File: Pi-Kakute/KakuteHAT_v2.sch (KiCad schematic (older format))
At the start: 52 parts, among them J1 40HAT, J10 Ext_Switch, J12 FC_Socket, J2 Conn_01x02, J3 I2C, J4 Mout, J6 RC_IN, J7 GPS2, J8 Power_Pad, J9 FC_Socket2, Q1 DMMT5401, Q2 DMG2305UX, SW1 Kakute Power Switch, SW2 Pi Power Switch, U1 TPS22810, U2 TPS709, U3 KakuteF4_V2, U4 TPS54331DR, U5 NC7SZ00P5X, U6 CAT24C32

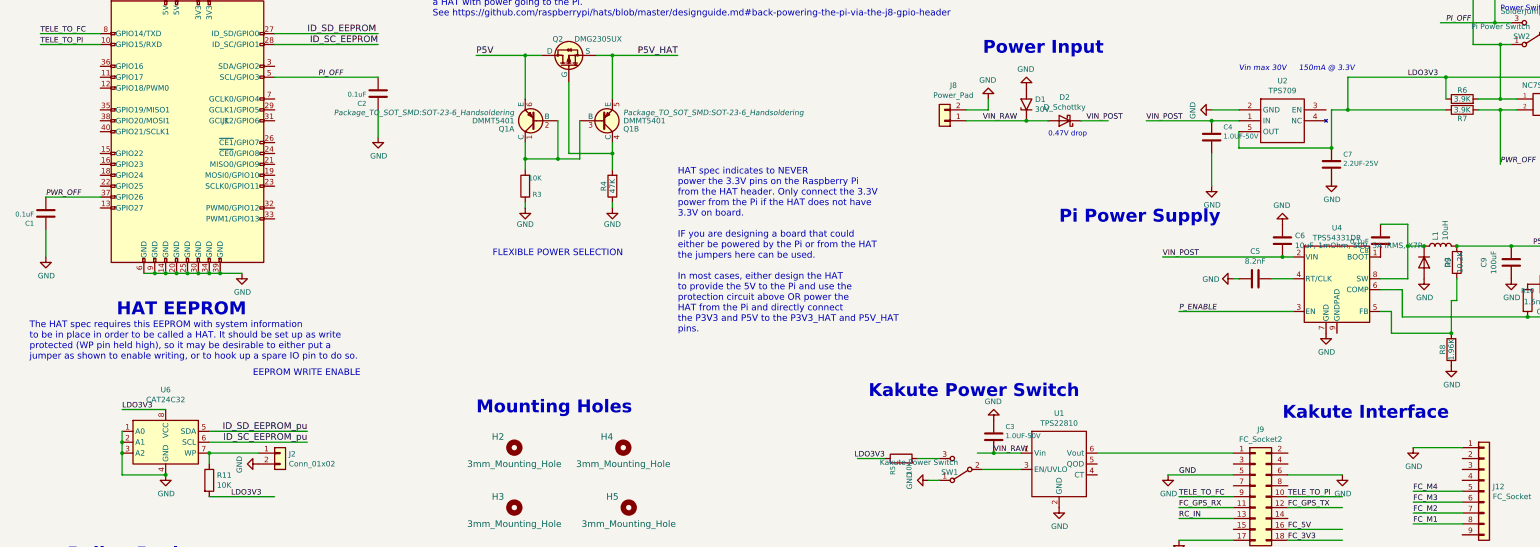
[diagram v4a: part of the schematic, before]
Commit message: Pi-Kakute: Label Cleanup
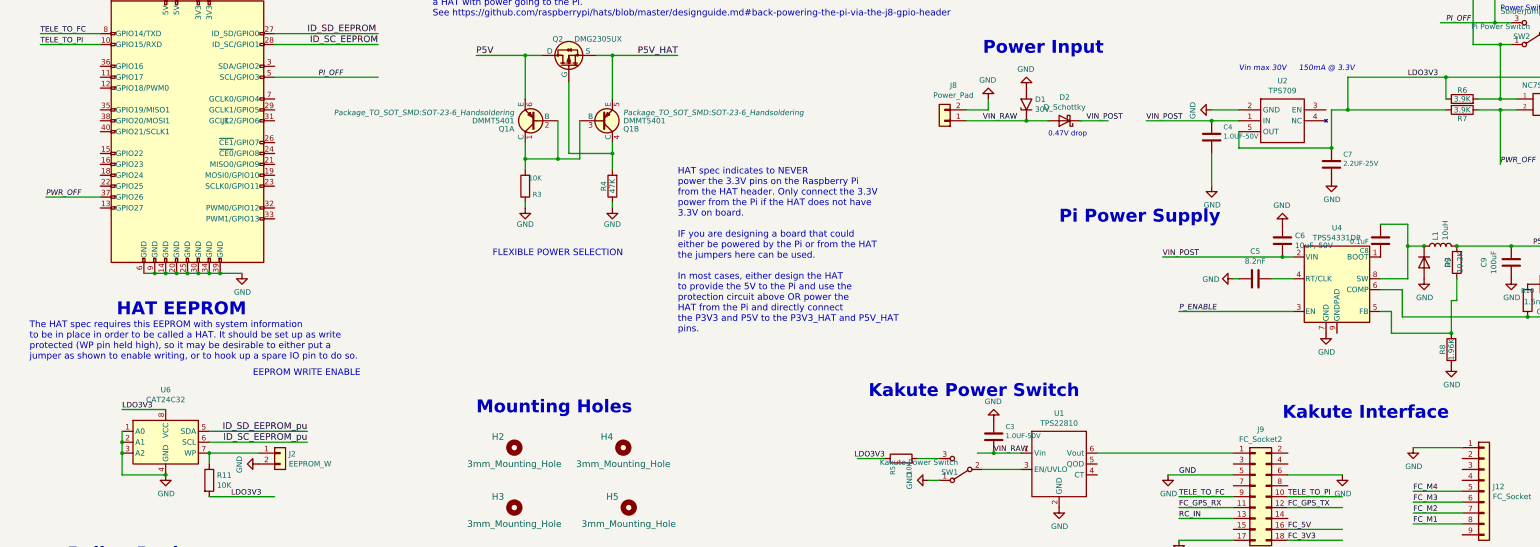
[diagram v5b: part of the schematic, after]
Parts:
- removed C1, C2: 0.1uF, Capacitor_SMD:C_0402_1005Metric, symbol Device:C
- C4: MPN CC0805KKX7R8BB105 -> CC0805KKX7R9BB105; SPN 311-1456-1-ND -> 311-1886-1-ND
- C6: value 10uF, 1mOhm, 50V, 5A IRMS, X7R -> 10uF, 50V
- H1, H2, H3, H4, H5, J10, J3, JP1: MFR (none) -> N/A; MPN (none) -> N/A; SPN (none) -> N/A; SPR (none) -> N/A
- J2: value Conn_01x02 -> EEPROM_W; MFR (none) -> N/A; MPN (none) -> N/A; SPN (none) -> N/A; SPR (none) -> N/A
- U2: MFR (none) -> TI; MPN (none) -> TPS70933DBVR; SPN (none) -> 296-35483-1-ND; SPR (none) -> Digikey
- U3: MFR HolyBro -> N/A; MPN (none) -> N/A; SPN (none) -> N/A; SPR (none) -> N/A
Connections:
- wire segments 168 -> 166
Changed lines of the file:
@@
 F 2 "MountingHole:MountingHole_3.2mm_M3_ISO7380" H 5550 6000 60  0001 C CNN
 F 3 "" H 5550 6000 60  0001 C CNN
-F 4 "~" H 0   0   50  0001 C CNN "MFR"
-F 5 "~" H 0   0   50  0001 C CNN "MPN"
+F 4 "N/A" H 0   0   50  0001 C CNN "MFR"
+F 5 "N/A" H 0   0   50  0001 C CNN "MPN"
+F 6 "N/A" H 5650 6000 50  0001 C CNN "SPN"
+F 7 "N/A" H 5650 6000 50  0001 C CNN "SPR"
 	1    5650 6000
 	1    0    0    -1
@@
 F 2 "MountingHole:MountingHole_3.2mm_M3_ISO7380" H 6550 6000 60  0001 C CNN
 F 3 "" H 6550 6000 60  0001 C CNN
-F 4 "~" H 0   0   50  0001 C CNN "MFR"
-F 5 "~" H 0   0   50  0001 C CNN "MPN"
+F 4 "N/A" H 0   0   50  0001 C CNN "MFR"
+F 5 "N/A" H 0   0   50  0001 C CNN "MPN"
+F 6 "N/A" H 6650 6000 50  0001 C CNN "SPN"
+F 7 "N/A" H 6650 6000 50  0001 C CNN "SPR"
 	1    6650 6000
 	1    0    0    -1
@@
 F 2 "MountingHole:MountingHole_3.2mm_M3_ISO7380" H 5550 6550 60  0001 C CNN
 F 3 "" H 5550 6550 60  0001 C CNN
-F 4 "~" H 0   0   50  0001 C CNN "MFR"
-F 5 "~" H 0   0   50  0001 C CNN "MPN"
+F 4 "N/A" H 0   0   50  0001 C CNN "MFR"
+F 5 "N/A" H 0   0   50  0001 C CNN "MPN"
+F 6 "N/A" H 5650 6550 50  0001 C CNN "SPN"
+F 7 "N/A" H 5650 6550 50  0001 C CNN "SPR"
 	1    5650 6550
 	1    0    0    -1
@@
 F 2 "MountingHole:MountingHole_3.2mm_M3_ISO7380" H 6600 6550 60  0001 C CNN
 F 3 "" H 6600 6550 60  0001 C CNN
-F 4 "~" H 0   0   50  0001 C CNN "MFR"
-F 5 "~" H 0   0   50  0001 C CNN "MPN"
+F 4 "N/A" H 0   0   50  0001 C CNN "MFR"
+F 5 "N/A" H 0   0   50  0001 C CNN "MPN"
+F 6 "N/A" H 6700 6550 50  0001 C CNN "SPN"
+F 7 "N/A" H 6700 6550 50  0001 C CNN "SPR"
 	1    6700 6550
 	1    0    0    -1
@@
 F 3 "" H 12050 3150 50  0001 C CNN
 F 4 "Yageo" H 150 -200 50  0001 C CNN "MFR"
-F 5 "CC0805KKX7R8BB105" H 150 -200 50  0001 C CNN "MPN"
-F 6 "311-1456-1-ND" H 150 -200 50  0001 C CNN "SPN"
+F 5 "CC0805KKX7R9BB105" H 150 -200 50  0001 C CNN "MPN"
+F 6 "311-1886-1-ND" H 150 -200 50  0001 C CNN "SPN"
 F 7 "OPL" H 150 -200 50  0001 C CNN "SPR"
 F 8 "302010179" H 400 -100 50  0001 C CNN "SKU"
@@
 F 2 "Kakute:Kakute F4 V2_NoPin" H 13250 7650 50  0001 C CNN
 F 3 "" H 13250 7650 50  0001 C CNN
-F 4 "HolyBro" H 550 1550 50  0001 C CNN "MFR"
-F 5 "~" H 0   0   50  0001 C CNN "MPN"
+F 4 "N/A" H 550 1550 50  0001 C CNN "MFR"
+F 5 "N/A" H 0   0   50  0001 C CNN "MPN"
+F 6 "N/A" H 12950 7800 50  0001 C CNN "SPN"
+F 7 "N/A" H 12950 7800 50  0001 C CNN "SPR"
 	1    12950 7800
 	1    0    0    -1
@@
 Wire Wire Line
 	1850 2300 1300 2300
-$Comp
-L Device:C C2
-U 1 1 5C476D9B
-P 4400 2750
-F 0 "C2" H 4508 2842 45  0000 L CNN
-F 1 "0.1uF" H 4508 2758 45  0000 L CNN
-F 2 "Capacitor_SMD:C_0402_1005Metric" H 4400 3000 20  0001 C CNN
-F 3 "" H 4400 2750 50  0001 C CNN
-F 4 "OPL" H -7500 -600 50  0001 C CNN "SPR"
-F 5 "CC0402KRX7R7BB104" H -6500 -1350 50  0001 C CNN "MPN"
-F 6 "302010138" H 0   0   50  0001 C CNN "SKU"
-F 7 "311-1338-1-ND" H 0   0   50  0001 C CNN "SPN"
-F 8 "Yageo" H 0   0   50  0001 C CNN "MFR"
-	1    4400 2750
-	-1   0    0    1
-$EndComp
-$Comp
-L Device:C C1
-U 1 1 5C476E84
-P 1350 3850
-F 0 "C1" H 1458 3942 45  0000 L CNN
-F 1 "0.1uF" H 1458 3858 45  0000 L CNN
-F 2 "Capacitor_SMD:C_0402_1005Metric" H 1350 4100 20  0001 C CNN
-F 3 "" H 1350 3850 50  0001 C CNN
-F 4 "OPL" H -10550 500 50  0001 C CNN "SPR"
-F 5 "CC0402KRX7R7BB104" H -9550 -250 50  0001 C CNN "MPN"
-F 6 "302010138" H 0   0   50  0001 C CNN "SKU"
-F 7 "311-1338-1-ND" H 0   0   50  0001 C CNN "SPN"
-F 8 "Yageo" H 0   0   50  0001 C CNN "MFR"
-	1    1350 3850
-	-1   0    0    1
-$EndComp
-Wire Wire Line
-	1350 4000 1350 4250
 Wire Wire Line
 	10300 6050 10050 6050
@@
 VIN_RAW
 Connection ~ 2700 7400
-Wire Wire Line
-	4400 2900 4400 3150
 Wire Wire Line
 	11750 6850 12250 6850
@@
 Wire Wire Line
 	8950 10600 8950 10650
-$Comp
-L power:GND #PWR04
-U 1 1 5C6346FB
-P 4400 3150
-F 0 "#PWR04" H 4400 2900 50  0001 C CNN
-F 1 "GND" H 4405 2977 50  0000 C CNN
-F 2 "" H 4400 3150 50  0001 C CNN
-F 3 "" H 4400 3150 50  0001 C CNN
-	1    4400 3150
-	1    0    0    -1
-$EndComp
-$Comp
-L power:GND #PWR01
-U 1 1 5C634769
-P 1350 4250
-F 0 "#PWR01" H 1350 4000 50  0001 C CNN
-F 1 "GND" H 1355 4077 50  0000 C CNN
-F 2 "" H 1350 4250 50  0001 C CNN
-F 3 "" H 1350 4250 50  0001 C CNN
-	1    1350 4250
-	1    0    0    -1
-$EndComp
 $Comp
 L power:GND #PWR02
@@
 P 12700 4100
 F 0 "C6" H 12585 4054 50  0000 R CNN
-F 1 "10uF, 1mOhm, 50V, 5A IRMS, X7R" H 12585 4145 50  0000 R CNN
+F 1 "10uF, 50V" H 12585 4145 50  0000 R CNN
 F 2 "Capacitor_SMD:C_1206_3216Metric" H 12738 3950 50  0001 C CNN
 F 3 "~" H 12700 4100 50  0001 C CNN
@@
 F 2 "MountingHole:MountingHole_2.2mm_M2_ISO7380" H 5600 7600 50  0001 C CNN
 F 3 "~" H 5600 7600 50  0001 C CNN
-F 4 "~" H 0   0   50  0001 C CNN "MFR"
-F 5 "~" H 0   0   50  0001 C CNN "MPN"
+F 4 "N/A" H 0   0   50  0001 C CNN "MFR"
+F 5 "N/A" H 0   0   50  0001 C CNN "MPN"
+F 6 "N/A" H 5600 7600 50  0001 C CNN "SPN"
+F 7 "N/A" H 5600 7600 50  0001 C CNN "SPR"
 	1    5600 7600
 	1    0    0    -1
@@
 F 2 "Connector_PinHeader_2.54mm:PinHeader_1x02_P2.54mm_Vertical" H 8950 9550 50  0001 C CNN
 F 3 "~" H 8950 9550 50  0001 C CNN
+F 4 "N/A" H 8950 9550 50  0001 C CNN "MFR"
+F 5 "N/A" H 8950 9550 50  0001 C CNN "MPN"
+F 6 "N/A" H 8950 9550 50  0001 C CNN "SPN"
+F 7 "N/A" H 8950 9550 50  0001 C CNN "SPR"
 	1    8950 9550
 	-1   0    0    1
@@
 P 3500 6050
 F 0 "J2" H 3580 6042 50  0000 L CNN
-F 1 "Conn_01x02" H 3580 5951 50  0000 L CNN
+F 1 "EEPROM_W" H 3580 5951 50  0000 L CNN
 F 2 "Connector_PinHeader_2.54mm:PinHeader_1x02_P2.54mm_Vertical" H 3500 6050 50  0001 C CNN
 F 3 "~" H 3500 6050 50  0001 C CNN
-F 4 "~" H 3500 6050 50  0001 C CNN "MFR"
-F 5 "~" H 3500 6050 50  0001 C CNN "MPN"
-F 6 "~" H 3500 6050 50  0001 C CNN "SPN"
-F 7 "~" H 3500 6050 50  0001 C CNN "SPR"
+F 4 "N/A" H 3500 6050 50  0001 C CNN "MFR"
+F 5 "N/A" H 3500 6050 50  0001 C CNN "MPN"
+F 6 "N/A" H 3500 6050 50  0001 C CNN "SPN"
+F 7 "N/A" H 3500 6050 50  0001 C CNN "SPR"
 	1    3500 6050
 	1    0    0    -1
@@
 F 2 "Package_TO_SOT_SMD:SOT-23-5_HandSoldering" H 12700 3000 50  0001 L CNN
 F 3 "" H 12700 3000 50  0001 L CNN
+F 4 "TI" H 12700 3000 50  0001 C CNN "MFR"
+F 5 "TPS70933DBVR" H 12700 3000 50  0001 C CNN "MPN"
+F 6 "296-35483-1-ND" H 12700 3000 50  0001 C CNN "SPN"
+F 7 "Digikey" H 12700 3000 50  0001 C CNN "SPR"
 	1    12700 3000
 	1    0    0    -1
@@
 F 2 "Jumper:SolderJumper-3_P1.3mm_Bridged2Bar12_Pad1.0x1.5mm" H 15700 1950 50  0001 C CNN
 F 3 "~" H 15700 1950 50  0001 C CNN
+F 4 "N/A" H 15700 1950 50  0001 C CNN "MFR"
+F 5 "N/A" H 15700 1950 50  0001 C CNN "MPN"
+F 6 "N/A" H 15700 1950 50  0001 C CNN "SPN"
+F 7 "N/A" H 15700 1950 50  0001 C CNN "SPR"
 	1    15700 1950
 	0    -1   -1   0
@@
 F 2 "Connector_PinHeader_2.54mm:PinHeader_1x03_P2.54mm_Vertical" H 14950 1650 50  0001 C CNN
 F 3 "~" H 14950 1650 50  0001 C CNN
+F 4 "N/A" H 14950 1650 50  0001 C CNN "MFR"
+F 5 "N/A" H 14950 1650 50  0001 C CNN "MPN"
+F 6 "N/A" H 14950 1650 50  0001 C CNN "SPN"
+F 7 "N/A" H 14950 1650 50  0001 C CNN "SPR"
 	1    14950 1650
 	1    0    0    -1
